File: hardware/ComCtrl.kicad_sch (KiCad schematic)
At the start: 8 parts, among them K1 G5V-2-DC12, K2 G5V-2-DC12, U6 H11AA1

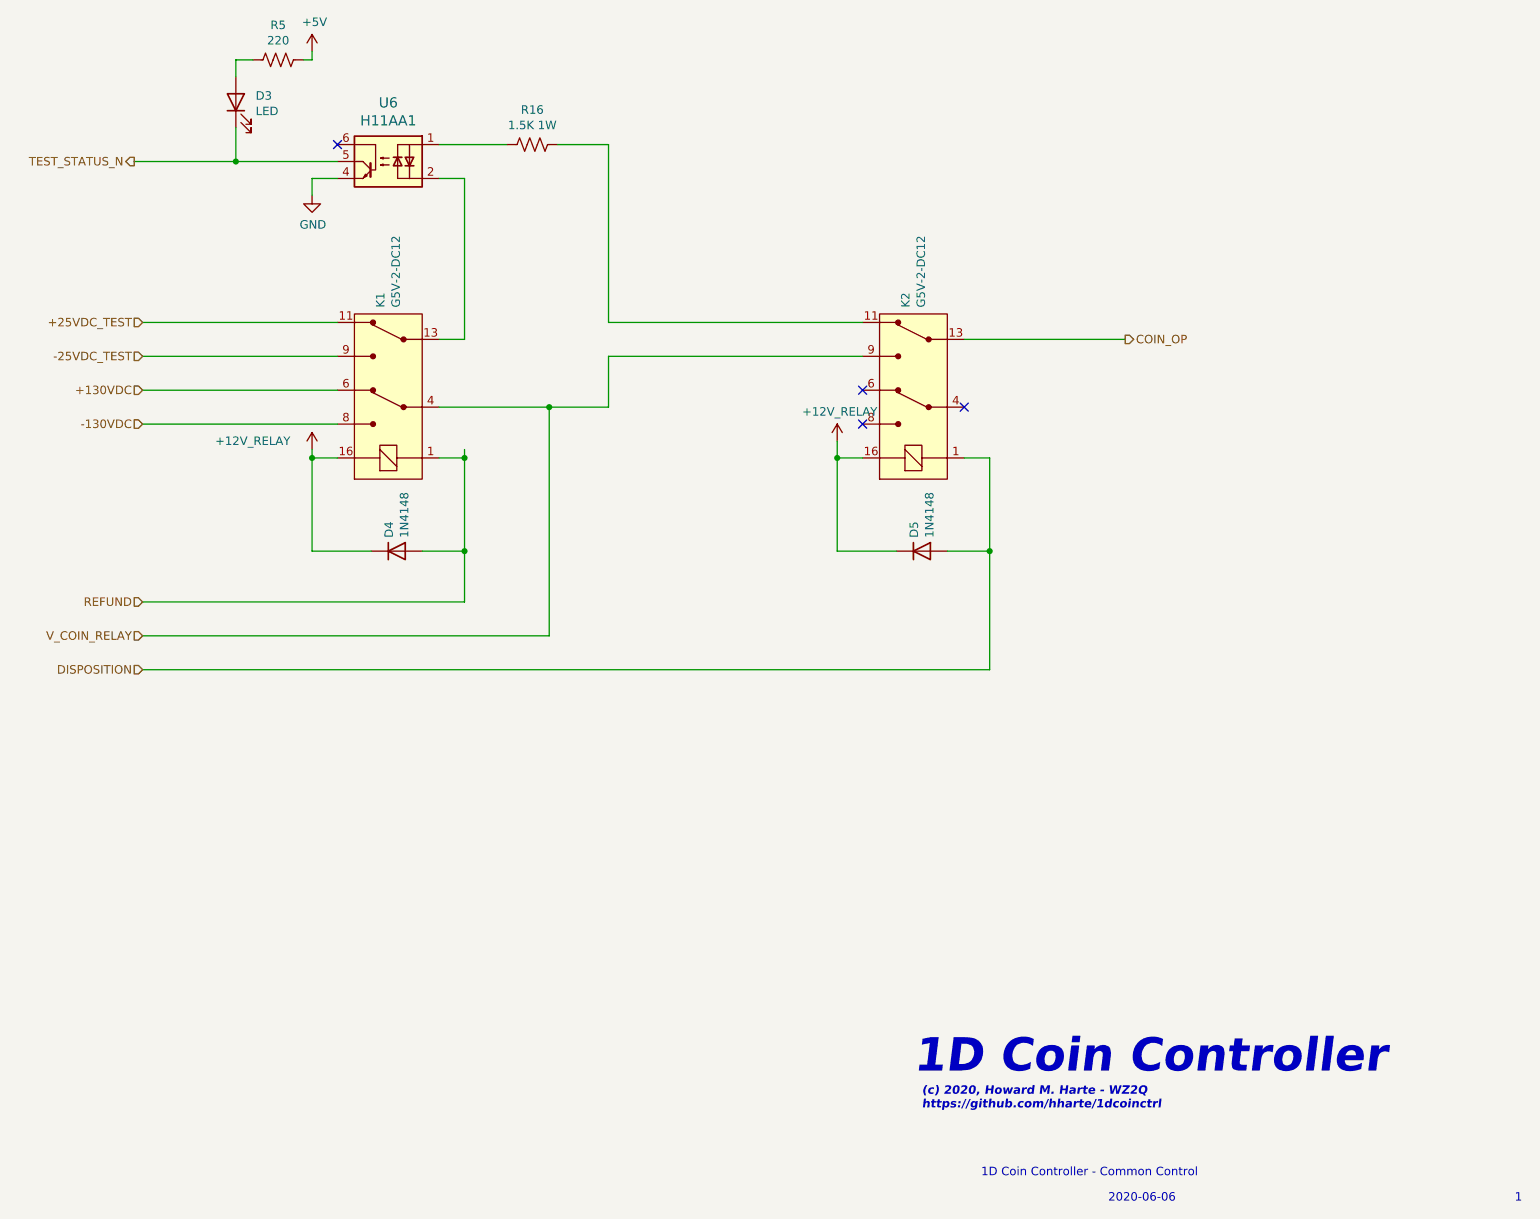
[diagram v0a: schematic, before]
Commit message: Issue 3:
* Remove barrel jack, replace with 4-position terminal block with
  provision for +/- 130VDC input in case the user already has an
  appropriate power supply and does not want the on-board
  DC-DC converter.  Note: 130V DC-DC converter PS2, relay
  K8, C14, D10, and R16 must be omitted during assembly.
* Add bi-color LEDs for line status.
  Green=Off-hook, normal polarity.
  Red=Off-hook, reverse polarity.
  Off=on-hook.
* Add header for FTDI USB UART, if user does not RS-232 UART levels.
  To use the FTDI header, do not populate U1 and other components on
  pp. 3 of the schematic.
* Remove i2c I/O expander and use PIC GPIOs directly.
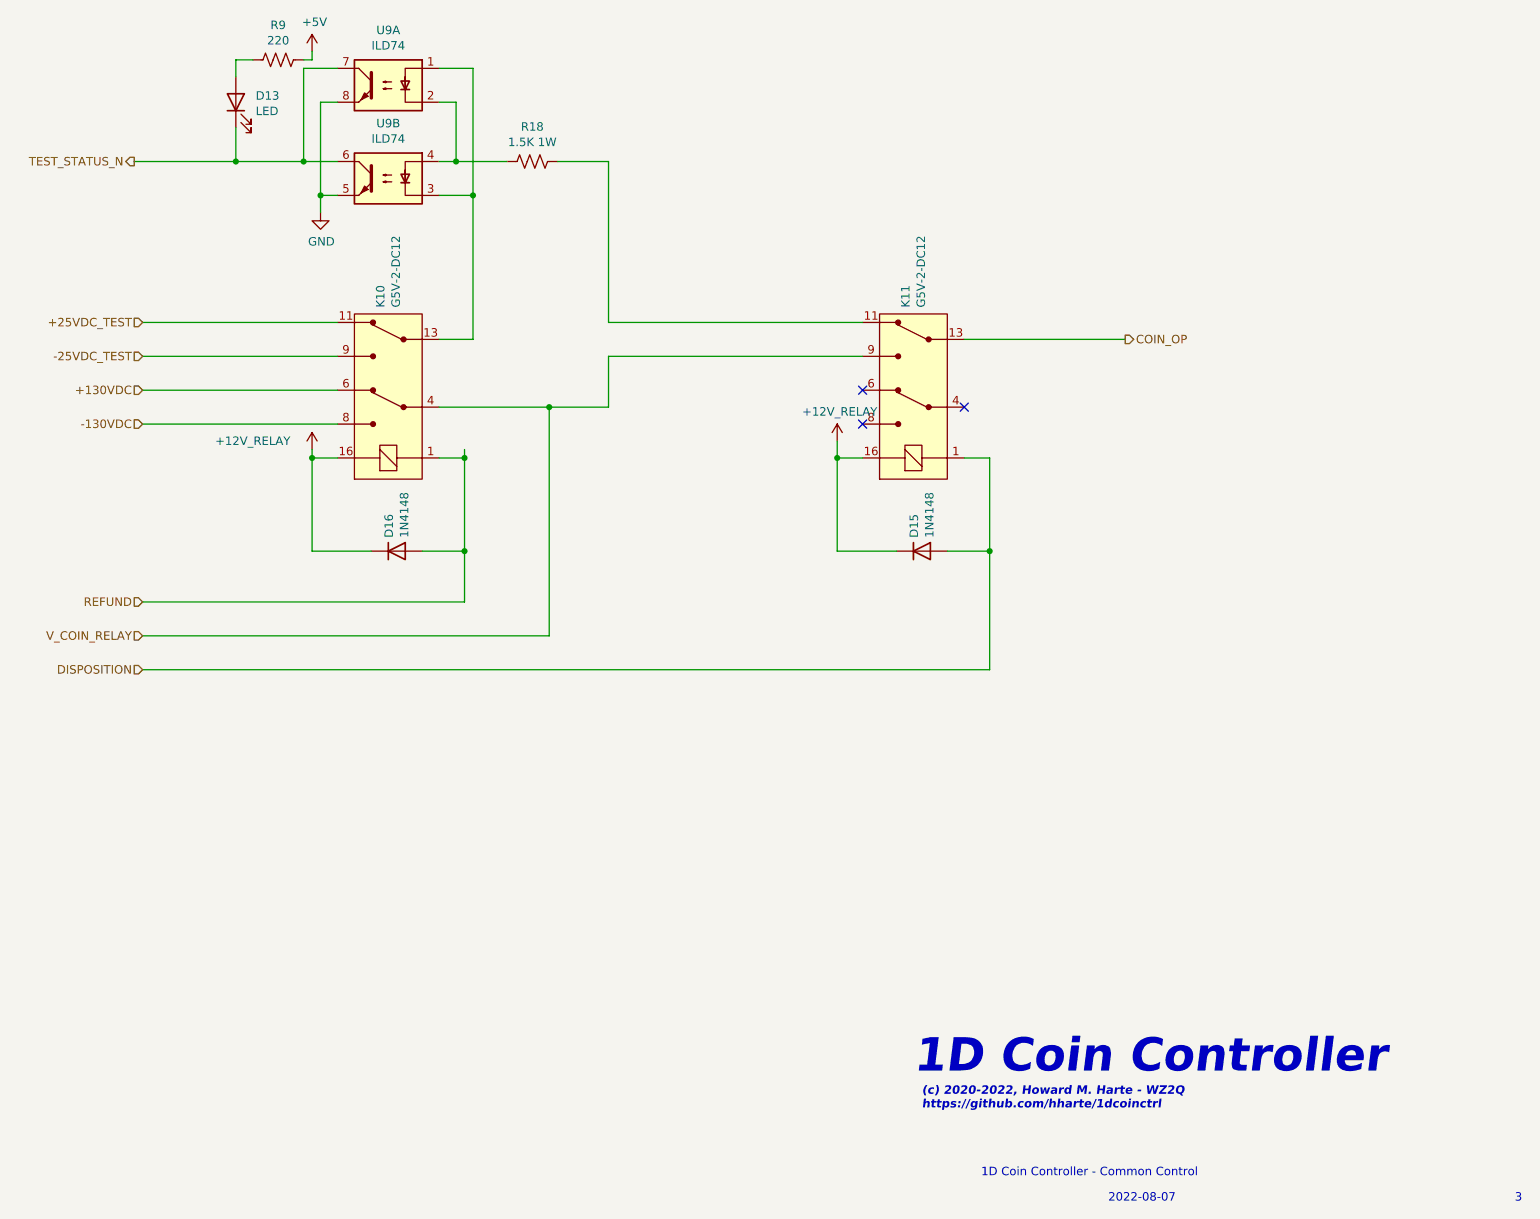
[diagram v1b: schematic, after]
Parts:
- removed U6: H11AA1, Package_DIP:DIP-6_W7.62mm, symbol Isolator:H11AA1
- added U9: ILD74, Package_DIP:DIP-8_W7.62mm_Socket, symbol Isolator:ILD74
- renumbered D3 to D13, D5 to D15, D4 to D16, K1 to K10, K2 to K11, R16 to R18, R5 to R9
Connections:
- net GND: now also U9.5, U9.8
- net TEST_STATUS_N: now also U9.6, U9.7
- net at K10.13 (COM2): now also U9.1, U9.3
- net at R18.2: now also U9.2, U9.4
- no-connect marks 4 -> 3
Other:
- note added: "(c) 2020-2022, Howard M. Harte - WZ2Q https://github.com/hharte/1dcoinctrl"
- note added: "2022-08-07"
- note added: "3"
- note removed: "(c) 2020, Howard M. Harte - WZ2Q https://github.com/hharte/1dcoinctrl"
- note removed: "1"
- note removed: "2020-06-06"
- moved on the sheet: R18

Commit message: Issue 4: Switch from PIC to AVR128DA28 MCU.
    * The AVR128DA28 is supported by the Arduino IDE.
    * Simpler UPDI programming.
    * Update to KiCAD 8.0.1
    * Fix footprint outline for IA1224S DC-DC converter.
    * Add initial Arduino firmware for AVR128DA28 MCU.
    * Move Earth Ground hole.
    * Add jumpers for UART and UPDI configuration.
    * Add 3D-printable end caps for Hammond enclosure.
    * Geographical reannotate PCB.
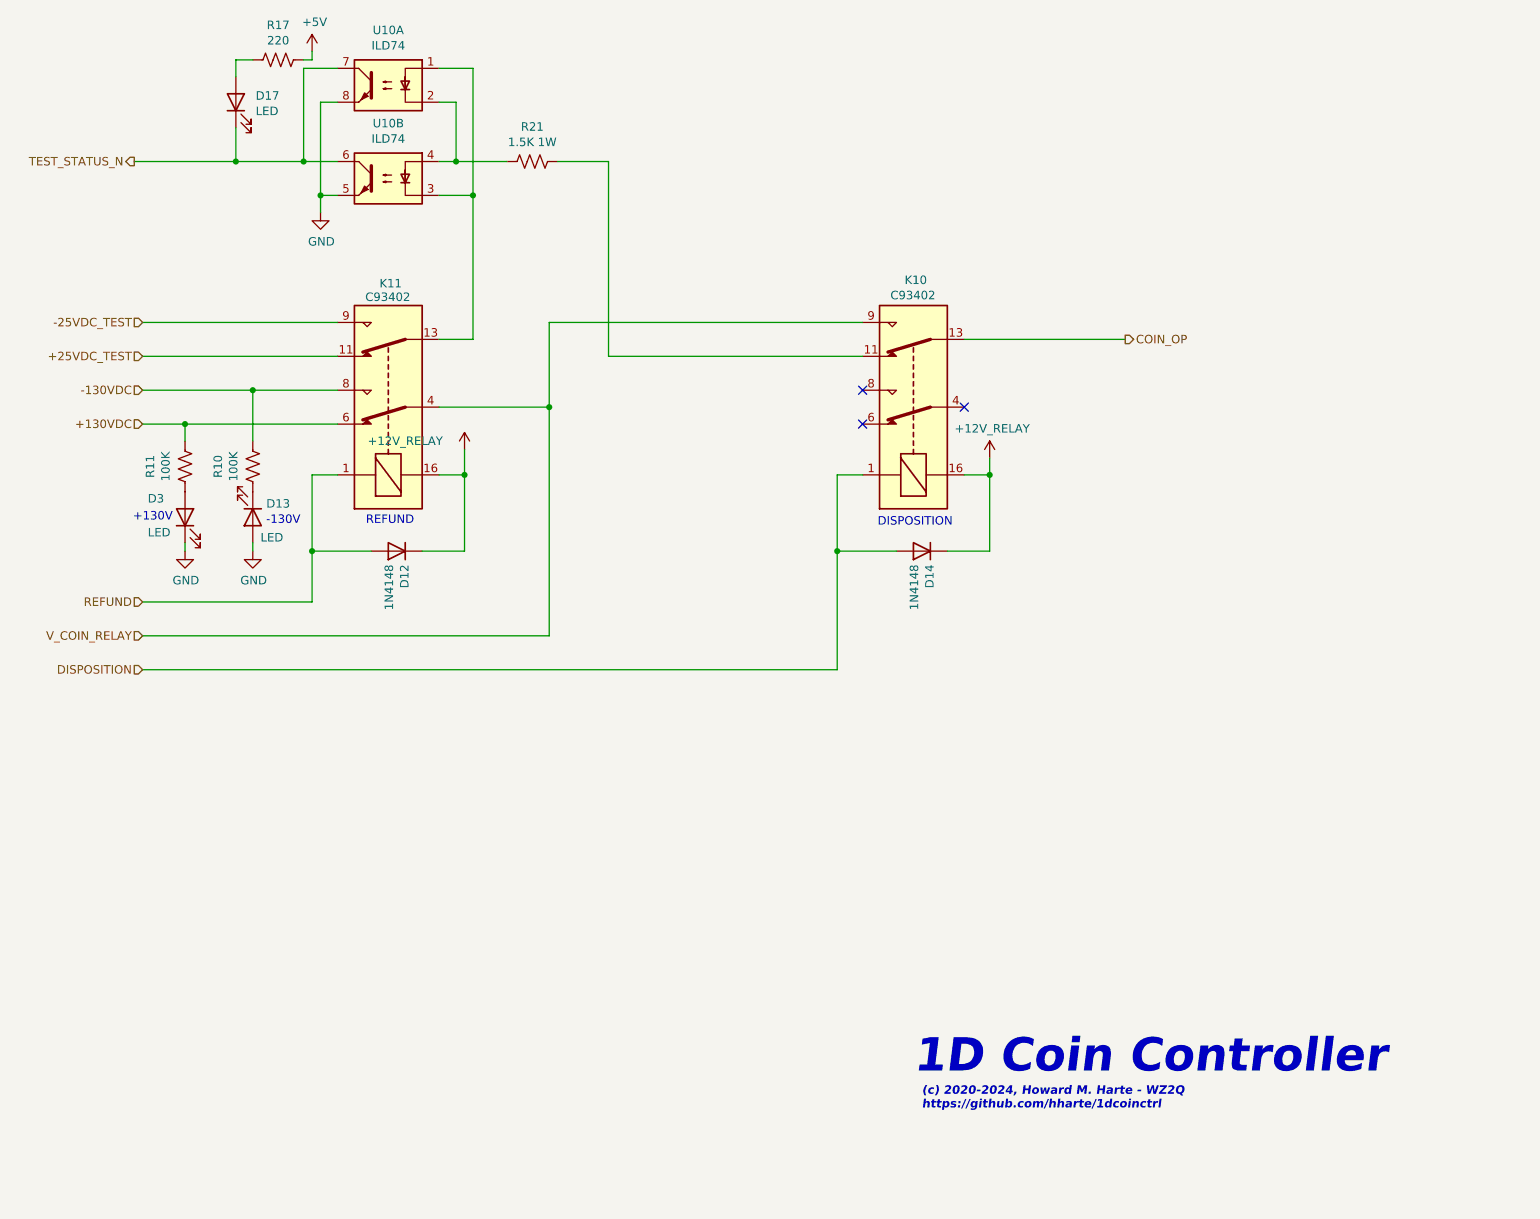
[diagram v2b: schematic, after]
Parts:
- added D13, D3: LED, LED_THT:LED_D5.0mm, symbol Device:LED
- added R10, R11: 100K, Resistor_THT:R_Axial_DIN0207_L6.3mm_D2.5mm_P7.62mm_Horizontal, symbol Device:R_US
- D12: renamed from D16; Digi-Key_PN (none) -> 1N4148TACT-ND; MPN (none) -> 1N4148TA
- D14: renamed from D15; Digi-Key_PN (none) -> 1N4148TACT-ND; MPN (none) -> 1N4148TA
- D17: renamed from D13; Digi-Key_PN (none) -> 1497-1031-ND; MPN (none) -> XLUR12D
- K10: renamed from K11; value G5V-2-DC12 -> C93402; footprint digikey-footprints:Relay_THT_G5V-2 -> Relay_THT:Relay_DPDT_Omron_G5V-2; symbol 1d_coinctrl_r2-rescue:G5V-2-DC12-dk_Signal-Relays-Up-to-2-Amps -> Relay:G5V-2; DK_Datasheet_Link http://omronfs.omron.com/en_US/ecb/products/pdf/en-g5v_2.pdf -> https://omronfs.omron.com/en_US/ecb/products/pdf/en-g5v_2.p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; Digi-Key_PN Z768-ND -> PB1125-ND; MPN G5V-2-DC12 -> C93402
- K11: renamed from K10; value G5V-2-DC12 -> C93402; footprint digikey-footprints:Relay_THT_G5V-2 -> Relay_THT:Relay_DPDT_Omron_G5V-2; symbol 1d_coinctrl_r2-rescue:G5V-2-DC12-dk_Signal-Relays-Up-to-2-Amps -> Relay:G5V-2; DK_Datasheet_Link http://omronfs.omron.com/en_US/ecb/products/pdf/en-g5v_2.pdf -> https://omronfs.omron.com/en_US/ecb/products/pdf/en-g5v_2.p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; Digi-Key_PN Z768-ND -> PB1125-ND; MPN G5V-2-DC12 -> C93402
- R17: renamed from R9; Digi-Key_PN (none) -> S220HCT-ND; MPN (none) -> CFM12JT220R
- R21: renamed from R18; Digi-Key_PN (none) -> PPC1.5KW-1CT-ND; MPN (none) -> PR01000101501JR500
- U10: renamed from U9; Digi-Key_PN (none) -> CNY74-2H-ND; MPN (none) -> CNY74-2H
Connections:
- net +130VDC: now also R11.1
- net -130VDC: now also R10.1
- net GND: now also D13.2 (A), D3.1 (K)
- new net: D13.1 (K), R10.2
- new net: D3.2 (A), R11.2
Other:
- note added: "(c) 2020-2024, Howard M. Harte - WZ2Q https://github.com/hharte/1dcoinctrl"
- note added: "+130V"
- note added: "-130V"
- note added: "DISPOSITION"
- note added: "REFUND"
- note removed: "(c) 2020-2022, Howard M. Harte - WZ2Q https://github.com/hharte/1dcoinctrl"
- note removed: "1D Coin Controller - Common Control"
- note removed: "2022-08-07"
- note removed: "3"
- title: (none) -> 1D Coin Controller - Common Control
- moved on the sheet: D12, D14
